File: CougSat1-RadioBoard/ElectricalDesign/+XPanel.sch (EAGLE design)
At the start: 68 parts, among them J1 ADCS Connector, J2 Low Gain +, J3 Low Gain -, J4 Low Gain Coax, J5 GPS Coax, J6 EPS Connector, U1 AD8515, U2 AD8542, U3 AD7291

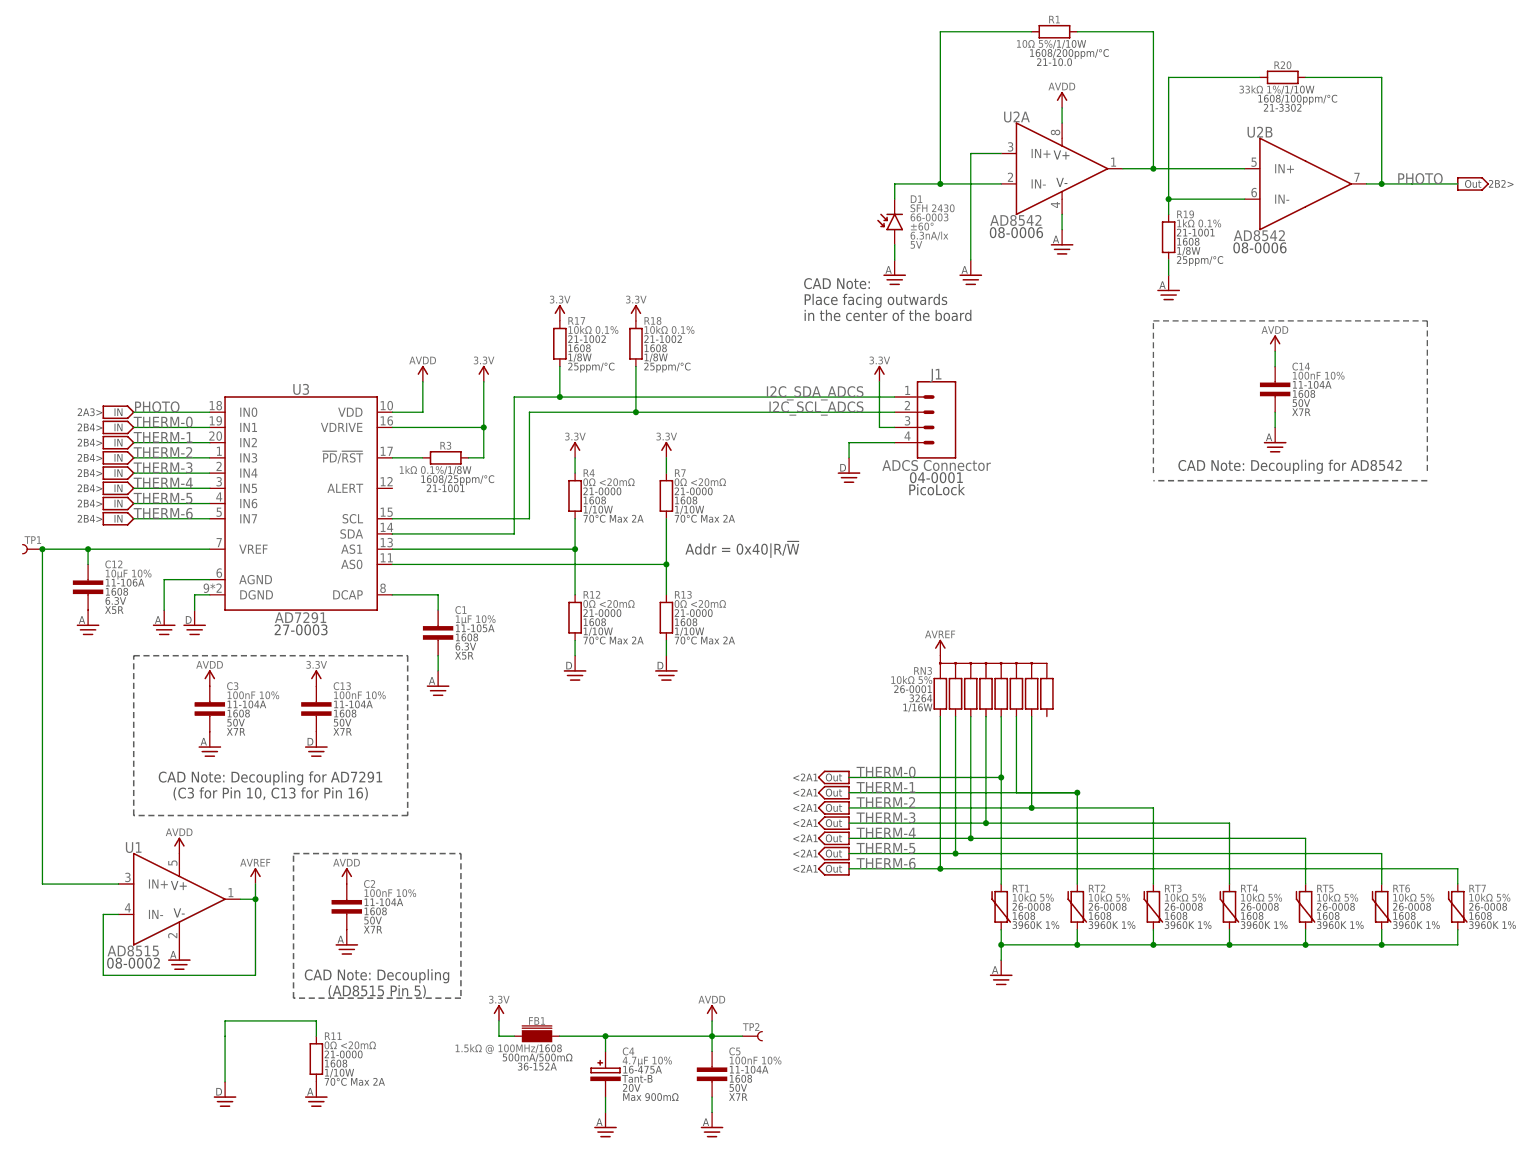
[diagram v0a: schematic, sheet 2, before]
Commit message: Fixed Spacing
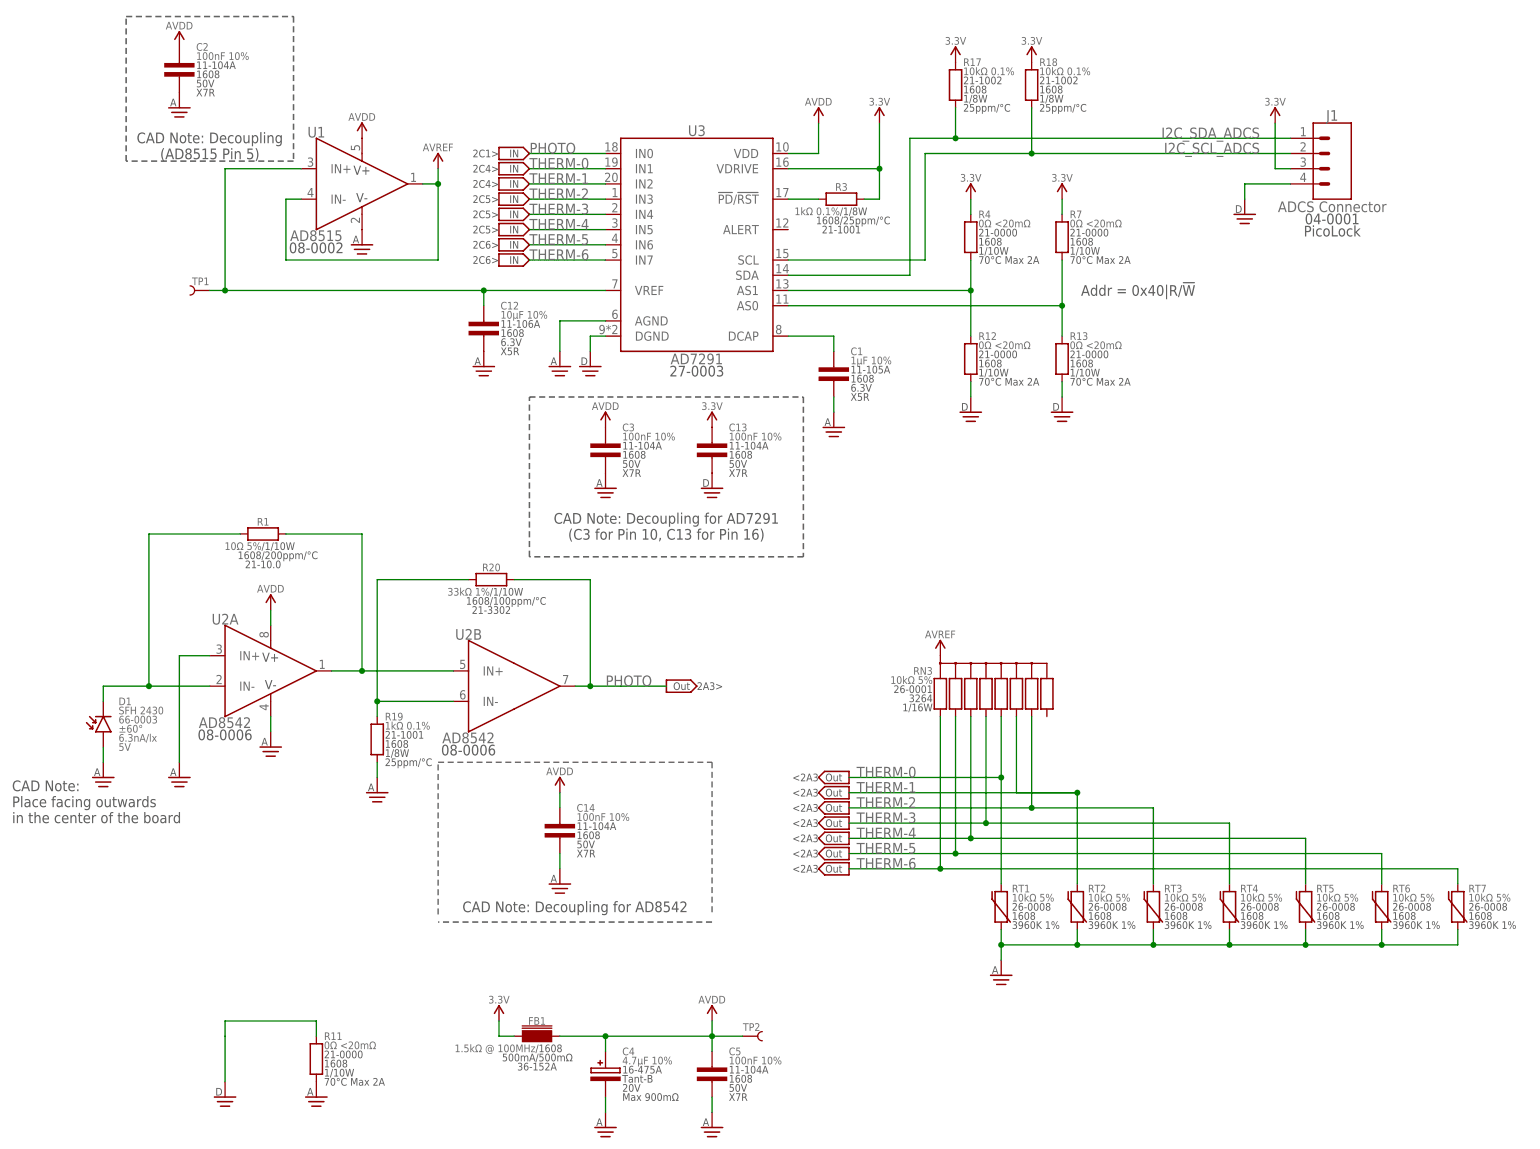
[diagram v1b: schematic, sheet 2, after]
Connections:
- net IN-1 renamed PHOTODIODE_IN-1
- net IN-2 renamed PHOTODIODE_IN-2
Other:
- note added: "2C1>"
- note added: "2C4>"
- note added: "2C5>"
- note added: "2C6>"
- note added: "<2A3"
- note removed: "2B2>"
- note removed: "2B4>"
- note removed: "<2A1"
- moved on the sheet: AE1, C1, C12, C13, C14, C2, C3, D1, H1, H2, H3, H4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

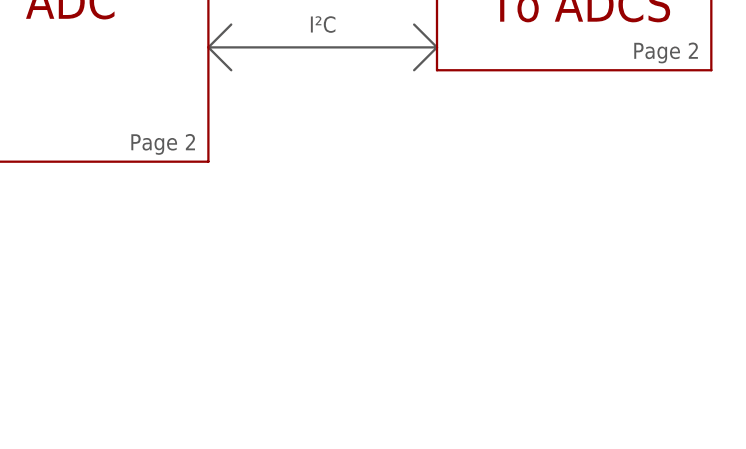
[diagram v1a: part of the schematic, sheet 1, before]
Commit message: Added Variant Label
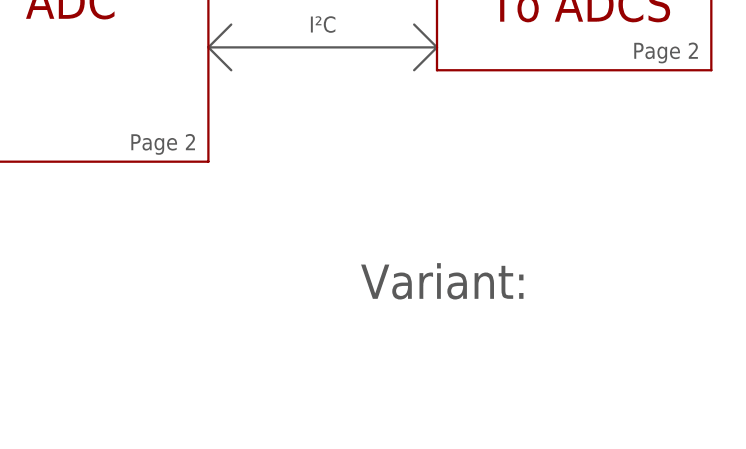
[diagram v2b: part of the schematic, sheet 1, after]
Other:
- note added: "Variant:"
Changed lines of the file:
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@@
 <text x="113.03" y="44.45" size="1.778" layer="97" align="bottom-right">Page 2</text>
 <text x="173.99" y="82.55" size="1.778" layer="97" align="bottom-right">Page 3</text>
+<text x="210.82" y="27.94" size="3.81" layer="97" align="bottom-right">Variant: </text>
+<text x="210.82" y="27.94" size="3.81" layer="97">&gt;ASSEMBLY_VARIANT</text>
 </plain>
 <instances>

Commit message: Exported Schematic
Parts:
- removed C14: 100nF 10%, CougsInSpace-Capacitors:CAP-V-100NF-1608
- removed R19: 1kΩ 0.1%, CougsInSpace-Resistors:RES-V-1K-1608
- removed R20: 33kΩ 1%, CougsInSpace-Resistors:RES-H-33K-1608
- removed U2: AD8542, CougsInSpace-IC-Amplifiers:OPAMP-2-AD8542-MSOP8
- R1: value 10Ω 5% -> 2kΩ 0.1%; device CougsInSpace-Resistors:RES-H-10R-1608 -> CougsInSpace-Resistors:RES-V-2K-1608
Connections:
- removed net OUT1_IN+2: R1.2, U2A.OUT, U2B.IN+
- removed net PHOTODIODE_IN-1: D1.C, R1.1, U2A.IN-
- removed net PHOTODIODE_IN-2: R19.2, R20.1, U2B.IN-
- net 3.3V: now also D1.C
- net AGND: now also R1.1; no longer C14.2, D1.A, R19.1, U2A.IN+, U2A.V-
- net AVDD: no longer C14.1, U2A.V+
- net PHOTO: now also D1.A, R1.2; no longer R20.2, U2B.OUT
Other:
- note added: "2A2>"
- note added: "2B1>"
- note added: "ADCS Picolock Connector"
- note added: "EPS Picolock Connector"
- note added: "GPS Coax"
- note added: "Low Gain Coax"
- note removed: "2A3>"
- note removed: "2C1>"
- note removed: "CAD Note: Decoupling for AD8542"
- moved on the sheet: D1

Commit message: Created mCAD and updated board reference designators and RF soldermask
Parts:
- removed R18: 10kΩ 0.1%, CougsInSpace-Resistors:RES-V-10K-1608
- added R10: 15Ω 5%, CougsInSpace-Resistors:RES-V-15R-THT-15MM
- C1: value 1µF 10% -> 100nF 10%; device CougsInSpace-Capacitors:CAP-V-1UF-1608 -> CougsInSpace-Capacitors:CAP-V-100NF-1608
- C12: value 10µF 10% -> 100nF 10%; device CougsInSpace-Capacitors:CAP-V-10UF-1608 -> CougsInSpace-Capacitors:CAP-V-100NF-1608
- C4: value 4.7µF 10% -> 100nF 10%; device CougsInSpace-Capacitors:CAP-POL-V-4.7UF-4028 -> CougsInSpace-Capacitors:CAP-V-100NF-1608
- C5: value 100nF 10% -> 1µF 10%; device CougsInSpace-Capacitors:CAP-V-100NF-1608 -> CougsInSpace-Capacitors:CAP-V-1UF-1608
- C6: value 100nF 10% -> 10µF 10%; device CougsInSpace-Capacitors:CAP-V-100NF-1608 -> CougsInSpace-Capacitors:CAP-V-10UF-1608
- C8: value 100nF 10% -> 4.7µF 10%; device CougsInSpace-Capacitors:CAP-V-100NF-1608 -> CougsInSpace-Capacitors:CAP-POL-V-4.7UF-4028
- H1, H2: value M2 -> M3; device CougsInSpace-Hardware:MOUNTING_HOLE-2.2 -> CougsInSpace-Hardware:MOUNTING_HOLE-3.3
- H10, H9: value M3 -> M2 Nut - 1mm; device CougsInSpace-Hardware:MOUNTING_HOLE-3.3 -> CougsInSpace-Hardware:MOUNTING_HOLE-1MM-M2_NUT
- H11, H12: value M2 Nut - 1mm -> M3; device CougsInSpace-Hardware:MOUNTING_HOLE-1MM-M2_NUT -> CougsInSpace-Hardware:MOUNTING_HOLE-3.3
- H7, H8: value M3 -> M2; device CougsInSpace-Hardware:MOUNTING_HOLE-3.3 -> CougsInSpace-Hardware:MOUNTING_HOLE-2.2
- J1: value ADCS Connector -> EPS Connector
- J2: value Low Gain + -> GPS Coax; device CougsInSpace-Connectors:1X01-THT-0.7 -> CougsInSpace-Connectors:COAX-U.FL
- J3: value Low Gain - -> Low Gain Coax; device CougsInSpace-Connectors:1X01-THT-0.7 -> CougsInSpace-Connectors:COAX-U.FL
- J4: value Low Gain Coax -> ADCS Connector; device CougsInSpace-Connectors:COAX-U.FL -> CougsInSpace-Connectors:1X04-PICOLOCK
- J5: value GPS Coax -> Low Gain +; device CougsInSpace-Connectors:COAX-U.FL -> CougsInSpace-Connectors:1X01-THT-0.7
- J6: value EPS Connector -> Low Gain -; device CougsInSpace-Connectors:1X04-PICOLOCK -> CougsInSpace-Connectors:1X01-THT-0.7
- R1: value 2kΩ 0.1% -> 0Ω <20mΩ; device CougsInSpace-Resistors:RES-V-2K-1608 -> CougsInSpace-Resistors:RES-V-0-1608
- R11: value 0Ω <20mΩ -> 15Ω 5%; device CougsInSpace-Resistors:RES-V-0-1608 -> CougsInSpace-Resistors:RES-V-15R-THT-15MM
- R16: value 0Ω <20mΩ -> 10kΩ 0.1%; device CougsInSpace-Resistors:RES-V-0-1608 -> CougsInSpace-Resistors:RES-V-10K-1608
- R3: value 1kΩ 0.1% -> 0Ω <20mΩ; device CougsInSpace-Resistors:RES-H-1K-1608 -> CougsInSpace-Resistors:RES-V-0-1608
- R7: value 0Ω <20mΩ -> 1kΩ 0.1%; device CougsInSpace-Resistors:RES-V-0-1608 -> CougsInSpace-Resistors:RES-H-1K-1608
- R8: value 15Ω 5% -> 2kΩ 0.1%; device CougsInSpace-Resistors:RES-V-15R-THT-15MM -> CougsInSpace-Resistors:RES-V-2K-1608
- R9: value 15Ω 5% -> 0Ω <20mΩ; device CougsInSpace-Resistors:RES-V-15R-THT-15MM -> CougsInSpace-Resistors:RES-V-0-1608
- renumbered RN3 to RN1, U3 to U2
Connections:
- net 3.3V: now also C7.1, J4.3, R16.2; no longer C13.1, J1.3, R18.2
- net ADC_AS0: now also R3.1, R5.2; no longer R13.2, R7.1
- net ADC_AS1: now also R6.2; no longer R12.2
- net AGND: now also C4.2, C6.2, C8.C, C9.2, R8.1, R9.1; no longer C1.2, C12.2, C2.2, C4.C, R1.1, R11.1
- net AVDD: now also C4.1, C8.A, C9.1; no longer C2.1, C4.A, C5.1
- net AVREF_UNBUF: now also C6.1; no longer C12.1
- net CHASSIS: now also C1.1, C12.1, C13.1, C2.1, H1.MOUNT, H11.MOUNT, H12.MOUNT, H2.MOUNT, R1.2, R12.2, R13.2; no longer C6.1, C7.1, C8.1, C9.1, H10.MOUNT, H7.MOUNT, H8.MOUNT, H9.MOUNT, R16.2, R5.2, R6.2
- net DCAP: now also C5.1; no longer C1.1
- net DGND: now also C7.2, J4.4, R5.1, R6.1, R9.2; no longer C13.2, J1.4, R11.2, R12.1, R13.1
- net GPS_COAX: now also J2.CENTER; no longer J5.CENTER
- net I2C_SCL_ADCS: now also J4.2, R16.1; no longer J1.2, R18.1
- net I2C_SDA_ADCS: now also J4.1; no longer J1.1
- net LOW_GAIN_COAX: now also J3.CENTER; no longer J4.CENTER
- net LOW_GAIN_N: now also J6.1; no longer J3.1
- net LOW_GAIN_P: now also J5.1; no longer J2.1
- net PD_RST: now also R7.1; no longer R3.1
- net PGND: now also C1.2, C12.2, C13.2, C2.2, H7.MOUNT, J1.4, R1.1, R10.1, R11.1, R12.1, R13.1; no longer C6.2, C7.2, C8.2, C9.2, H3.MOUNT, J6.4, R16.1, R5.1, R6.1, R8.1, R9.1
- net PHOTO: now also R8.2; no longer R1.2
- net RFGND-0: now also H10.MOUNT, H9.MOUNT, J3.SHIELD; no longer H11.MOUNT, H12.MOUNT, J4.SHIELD
- net RFGND-1: now also J2.SHIELD; no longer J5.SHIELD
- net SENSE: now also H3.MOUNT, H8.MOUNT, J1.3; no longer H1.MOUNT, H2.MOUNT, J6.3
- net THERM-0: now also RT4.2; no longer RT1.2
- net THERM-1: now also RT5.2; no longer RT2.2
- net THERM-2: now also RT7.2; no longer RT3.2
- net THERM-3: now also RT6.2; no longer RT4.2
- net THERM-4: now also RT2.2; no longer RT5.2
- net THERM-5: now also RT1.2; no longer RT6.2
- net THERM-6: now also RT3.2; no longer RT7.2
- net VCC: now also J1.1, J1.2, R10.2, R11.2; no longer J6.1, J6.2, R8.2, R9.2
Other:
- moved on the sheet: C10, C11, C3, C5, H1, H10, H11, H12, H2, H3, H5, H6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

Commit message: Photodiode Test
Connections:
- net VCC renamed DEPLOYABLE
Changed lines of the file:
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@@
 <?xml version="1.0" encoding="utf-8"?>
 <!DOCTYPE eagle SYSTEM "eagle.dtd">
-<eagle version="9.5.1">
+<eagle version="9.5.2">
 <drawing>
 <settings>
@@
 <setting verticaltext="up"/>
 </settings>
-<grid distance="0.5" unitdist="mm" unit="mm" style="lines" multiple="1" display="no" altdistance="0.01" altunitdist="inch" altunit="inch"/>
+<grid distance="0.1" unitdist="inch" unit="inch" style="lines" multiple="1" display="no" altdistance="0.01" altunitdist="inch" altunit="inch"/>
 <layers>
 <layer number="1" name="Top" color="4" fill="1" visible="no" active="no"/>
@@
 </segment>
 </net>
-<net name="VCC" class="0">
+<net name="DEPLOYABLE" class="0">
 <segment>
 <pinref part="J1" gate="G$1" pin="1"/>

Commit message: Changed resistors
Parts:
- R10, R11: value 15Ω 5% -> 5Ω 1%; device CougsInSpace-Resistors:RES-V-15R-THT-15MM -> CougsInSpace-Resistors:RES-V-5R-THT-15MM
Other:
- moved on the sheet: R10, R11
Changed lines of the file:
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@@
 <part name="H4" library="CougsInSpace-Hardware" deviceset="MOUNTING_HOLE" device="-2.2" value="M2"/>
 <part name="J1" library="CougsInSpace-Connectors" deviceset="1X04" device="-PICOLOCK" value="EPS Connector"/>
-<part name="R11" library="CougsInSpace-Resistors" deviceset="RES-V" device="-THT-15MM" technology="-15R" value="15Ω 5%"/>
-<part name="R10" library="CougsInSpace-Resistors" deviceset="RES-V" device="-THT-15MM" technology="-15R" value="15Ω 5%"/>
 <part name="SUPPLY18" library="CougsInSpace-PowerSymbols" deviceset="PGND" device=""/>
 <part name="FRAME4" library="CougsInSpace-Aesthetics" deviceset="FRAME-A" device="">
@@
 <part name="SUPPLY9" library="CougsInSpace-PowerSymbols" deviceset="3.3V" device=""/>
 <part name="OFFSHEET5" library="CougsInSpace-Aesthetics" deviceset="OFF_SHEET-OUT" device=""/>
+<part name="R10" library="CougsInSpace-Resistors" deviceset="RES-V" device="-THT-15MM" technology="-5R" value="5Ω 1%"/>
+<part name="R11" library="CougsInSpace-Resistors" deviceset="RES-V" device="-THT-15MM" technology="-5R" value="5Ω 1%"/>
 </parts>
 <sheets>
@@
 <attribute name="PACKAGE" x="188.595" y="124.206" size="1.778" layer="97" align="center"/>
 </instance>
-<instance part="R11" gate="G$1" x="208.28" y="132.08" smashed="yes">
-<attribute name="NAME" x="209.55" y="137.16" size="1.27" layer="95" align="center-left"/>
-<attribute name="VALUE" x="209.55" y="135.636" size="1.27" layer="96" align="center-left"/>
-<attribute name="PACKAGE" x="209.55" y="132.588" size="1.27" layer="97" align="center-left"/>
-<attribute name="POWER" x="209.55" y="131.064" size="1.27" layer="97" align="center-left"/>
-<attribute name="TEMP" x="209.55" y="129.54" size="1.27" layer="97" align="center-left"/>
-<attribute name="SKU" x="209.55" y="134.112" size="1.27" layer="97" align="center-left"/>
-</instance>
-<instance part="R10" gate="G$1" x="223.52" y="132.08" smashed="yes">
-<attribute name="NAME" x="224.79" y="137.16" size="1.27" layer="95" align="center-left"/>
-<attribute name="VALUE" x="224.79" y="135.636" size="1.27" layer="96" align="center-left"/>
-<attribute name="PACKAGE" x="224.79" y="132.588" size="1.27" layer="97" align="center-left"/>
-<attribute name="POWER" x="224.79" y="131.064" size="1.27" layer="97" align="center-left"/>
-<attribute name="TEMP" x="224.79" y="129.54" size="1.27" layer="97" align="center-left"/>
-<attribute name="SKU" x="224.79" y="134.112" size="1.27" layer="97" align="center-left"/>
-</instance>
 <instance part="SUPPLY18" gate="G$1" x="208.28" y="121.92" smashed="yes"/>
 <instance part="H11" gate="G$1" x="30.48" y="83.82" smashed="yes" rot="MR0">
@@
 </instance>
 <instance part="SUPPLY58" gate="G$1" x="203.2" y="93.98" smashed="yes"/>
+<instance part="R10" gate="G$1" x="208.28" y="132.08" smashed="yes">
+<attribute name="NAME" x="209.55" y="137.16" size="1.27" layer="95" align="center-left"/>
+<attribute name="VALUE" x="209.55" y="135.636" size="1.27" layer="96" align="center-left"/>
+<attribute name="PACKAGE" x="209.55" y="132.588" size="1.27" layer="97" align="center-left"/>
+<attribute name="POWER" x="209.55" y="131.064" size="1.27" layer="97" align="center-left"/>
+<attribute name="TEMP" x="209.55" y="129.54" size="1.27" layer="97" align="center-left"/>
+<attribute name="SKU" x="209.55" y="134.112" size="1.27" layer="97" align="center-left"/>
+</instance>
+<instance part="R11" gate="G$1" x="223.52" y="132.08" smashed="yes">
+<attribute name="NAME" x="224.79" y="137.16" size="1.27" layer="95" align="center-left"/>
+<attribute name="VALUE" x="224.79" y="135.636" size="1.27" layer="96" align="center-left"/>
+<attribute name="PACKAGE" x="224.79" y="132.588" size="1.27" layer="97" align="center-left"/>
+<attribute name="POWER" x="224.79" y="131.064" size="1.27" layer="97" align="center-left"/>
+<attribute name="TEMP" x="224.79" y="129.54" size="1.27" layer="97" align="center-left"/>
+<attribute name="SKU" x="224.79" y="134.112" size="1.27" layer="97" align="center-left"/>
+</instance>
 </instances>
 <busses>
@@
 <pinref part="J1" gate="G$1" pin="1"/>
 <wire x1="195.58" y1="139.7" x2="198.12" y2="139.7" width="0.1524" layer="91"/>
-<pinref part="R11" gate="G$1" pin="2"/>
 <wire x1="198.12" y1="139.7" x2="208.28" y2="139.7" width="0.1524" layer="91"/>
 <wire x1="208.28" y1="139.7" x2="208.28" y2="137.16" width="0.1524" layer="91"/>
 <wire x1="208.28" y1="139.7" x2="223.52" y2="139.7" width="0.1524" layer="91"/>
 <junction x="208.28" y="139.7"/>
-<pinref part="R10" gate="G$1" pin="2"/>
 <wire x1="223.52" y1="139.7" x2="223.52" y2="137.16" width="0.1524" layer="91"/>
 <pinref part="J1" gate="G$1" pin="2"/>
@@
 <wire x1="198.12" y1="137.16" x2="198.12" y2="139.7" width="0.1524" layer="91"/>
 <junction x="198.12" y="139.7"/>
+<pinref part="R10" gate="G$1" pin="2"/>
+<pinref part="R11" gate="G$1" pin="2"/>
 </segment>
 </net>
@@
 <segment>
 <pinref part="SUPPLY18" gate="G$1" pin="PGND"/>
-<pinref part="R11" gate="G$1" pin="1"/>
 <wire x1="208.28" y1="129.54" x2="208.28" y2="127" width="0.1524" layer="91"/>
 <pinref part="J1" gate="G$1" pin="4"/>
@@
 <wire x1="198.12" y1="127" x2="208.28" y2="127" width="0.1524" layer="91"/>
 <junction x="208.28" y="127"/>
-<pinref part="R10" gate="G$1" pin="1"/>
 <wire x1="223.52" y1="129.54" x2="223.52" y2="127" width="0.1524" layer="91"/>
 <wire x1="208.28" y1="127" x2="223.52" y2="127" width="0.1524" layer="91"/>
-</segment>
-<segment>
+<pinref part="R10" gate="G$1" pin="1"/>
+<pinref part="R11" gate="G$1" pin="1"/>
+</segment>
+<segment>
